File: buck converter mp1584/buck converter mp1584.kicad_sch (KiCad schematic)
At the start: 19 parts, among them J1 VIN, J2 GND, J3 VOUT, J4 GND

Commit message: First rough draft
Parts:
- added U1: ~, symbol buck converter module:mp1584
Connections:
- net FB: now also U1.4 (FB)
- net at C1.2, C11.2, C2.2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: now also U1.5 (GND)
- net at C1.1, C11.1, J1.1 (Pin_1)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: now also U1.7 (VIN)
- net BST: no longer names the net of C4.2
- net BST: now also U1.8 (BST)
- net COMP: no longer names the net of C3.1
- net COMP: now also U1.3 (COMP)
- net ENABLE: no longer names the net of R5.2, R6.1
- net ENABLE: now also U1.2 (EN)
- net FREQ: no longer names the net of R4.1
- net FREQ: now also U1.6 (FREQ)
- net SW: no longer names the net of C4.1, D1.1 (K), L1.1
- net SW: now also U1.1 (SW)
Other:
- moved on the sheet: R4, R5
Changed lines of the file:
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@@
   (junction (at 222.25 154.94) (diameter 0) (color 0 0 0 0)
   )
-  (junction (at 92.71 154.94) (diameter 0) (color 0 0 0 0)
+  (junction (at 78.74 154.94) (diameter 0) (color 0 0 0 0)
   )
   (junction (at 198.12 59.69) (diameter 0) (color 0 0 0 0)
@@
   (junction (at 49.53 154.94) (diameter 0) (color 0 0 0 0)
   )
-  (junction (at 63.5 105.41) (diameter 0) (color 0 0 0 0)
+  (junction (at 63.5 59.69) (diameter 0) (color 0 0 0 0)
   )
   (junction (at 198.12 154.94) (diameter 0) (color 0 0 0 0)
@@
   (junction (at 161.29 154.94) (diameter 0) (color 0 0 0 0)
   )
+  (junction (at 100.33 154.94) (diameter 0) (color 0 0 0 0)
+  )
   (junction (at 63.5 154.94) (diameter 0) (color 0 0 0 0)
   )
+  (junction (at 63.5 86.36) (diameter 0) (color 0 0 0 0)
+  )
   (no_connect (at 186.69 96.52))
-  (wire (pts (xy 92.71 115.57) (xy 92.71 124.46))
-    (stroke (width 0) (type default))
-  )
-  (wire (pts (xy 63.5 105.41) (xy 71.12 105.41))
+  (wire (pts (xy 78.74 99.06) (xy 78.74 124.46))
     (stroke (width 0) (type default))
   )
@@
     (stroke (width 0) (type default))
   )
-  (wire (pts (xy 144.78 82.55) (xy 133.35 82.55))
-    (stroke (width 0) (type default))
-  )
   (wire (pts (xy 186.69 59.69) (xy 198.12 59.69))
     (stroke (width 0) (type default))
@@
     (stroke (width 0) (type default))
   )
-  (wire (pts (xy 138.43 111.76) (xy 137.16 111.76))
+  (wire (pts (xy 144.78 92.71) (xy 113.03 92.71))
     (stroke (width 0) (type default))
   )
@@
     (stroke (width 0) (type default))
   )
-  (wire (pts (xy 63.5 85.09) (xy 63.5 105.41))
-    (stroke (width 0) (type default))
-  )
-  (wire (pts (xy 92.71 132.08) (xy 92.71 154.94))
+  (wire (pts (xy 100.33 154.94) (xy 138.43 154.94))
+    (stroke (width 0) (type default))
+  )
+  (wire (pts (xy 78.74 132.08) (xy 78.74 154.94))
+    (stroke (width 0) (type default))
+  )
+  (wire (pts (xy 63.5 59.69) (xy 100.33 59.69))
+    (stroke (width 0) (type default))
+  )
+  (wire (pts (xy 63.5 86.36) (xy 87.63 86.36))
     (stroke (width 0) (type default))
   )
@@
     (stroke (width 0) (type default))
   )
-  (wire (pts (xy 138.43 120.65) (xy 138.43 111.76))
+  (wire (pts (xy 138.43 99.06) (xy 138.43 120.65))
     (stroke (width 0) (type default))
   )
@@
     (stroke (width 0) (type default))
   )
-  (wire (pts (xy 63.5 59.69) (xy 63.5 77.47))
+  (wire (pts (xy 63.5 59.69) (xy 63.5 68.58))
     (stroke (width 0) (type default))
   )
@@
     (stroke (width 0) (type default))
   )
-  (wire (pts (xy 63.5 154.94) (xy 92.71 154.94))
+  (wire (pts (xy 63.5 154.94) (xy 78.74 154.94))
     (stroke (width 0) (type default))
   )
@@
     (stroke (width 0) (type default))
   )
+  (wire (pts (xy 113.03 99.06) (xy 138.43 99.06))
+    (stroke (width 0) (type default))
+  )
   (wire (pts (xy 36.83 154.94) (xy 49.53 154.94))
     (stroke (width 0) (type default))
@@
     (stroke (width 0) (type default))
   )
+  (wire (pts (xy 63.5 86.36) (xy 63.5 123.19))
+    (stroke (width 0) (type default))
+  )
+  (wire (pts (xy 100.33 59.69) (xy 100.33 77.47))
+    (stroke (width 0) (type default))
+  )
   (wire (pts (xy 27.94 59.69) (xy 36.83 59.69))
     (stroke (width 0) (type default))
@@
     (stroke (width 0) (type default))
   )
-  (wire (pts (xy 92.71 154.94) (xy 138.43 154.94))
+  (wire (pts (xy 133.35 86.36) (xy 113.03 86.36))
+    (stroke (width 0) (type default))
+  )
+  (wire (pts (xy 100.33 107.95) (xy 100.33 154.94))
+    (stroke (width 0) (type default))
+  )
+  (wire (pts (xy 78.74 154.94) (xy 100.33 154.94))
     (stroke (width 0) (type default))
   )
@@
     (stroke (width 0) (type default))
   )
-  (wire (pts (xy 144.78 74.93) (xy 144.78 82.55))
+  (wire (pts (xy 81.28 92.71) (xy 87.63 92.71))
+    (stroke (width 0) (type default))
+  )
+  (wire (pts (xy 133.35 59.69) (xy 133.35 86.36))
+    (stroke (width 0) (type default))
+  )
+  (wire (pts (xy 144.78 74.93) (xy 144.78 92.71))
     (stroke (width 0) (type default))
   )
@@
     (stroke (width 0) (type default))
   )
-  (wire (pts (xy 63.5 105.41) (xy 63.5 123.19))
+  (wire (pts (xy 78.74 99.06) (xy 87.63 99.06))
+    (stroke (width 0) (type default))
+  )
+  (wire (pts (xy 63.5 76.2) (xy 63.5 86.36))
     (stroke (width 0) (type default))
   )
@@
     (stroke (width 0) (type default))
   )
-  (global_label "BST" (shape input) (at 133.35 82.55 180) (fields_autoplaced)
+  (global_label "FB" (shape input) (at 81.28 92.71 180) (fields_autoplaced)
     (effects (font (size 1.27 1.27)) (justify right))
-    (property "Intersheetrefs" "${INTERSHEET_REFS}" (at 126.9177 82.55 0)
+    (property "Intersheetrefs" "${INTERSHEET_REFS}" (at 75.9362 92.71 0)
       (effects (font (size 1.27 1.27)) (justify right) hide)
     )
@@
     )
   )
-  (global_label "ENABLE" (shape input) (at 71.12 105.41 0) (fields_autoplaced)
-    (effects (font (size 1.27 1.27)) (justify left))
-    (property "Intersheetrefs" "${INTERSHEET_REFS}" (at 81.1204 105.41 0)
-      (effects (font (size 1.27 1.27)) (justify left) hide)
-    )
-  )
-  (global_label "FREQ" (shape input) (at 92.71 115.57 0) (fields_autoplaced)
-    (effects (font (size 1.27 1.27)) (justify left))
-    (property "Intersheetrefs" "${INTERSHEET_REFS}" (at 100.5333 115.57 0)
-      (effects (font (size 1.27 1.27)) (justify left) hide)
-    )
-  )
-  (global_label "COMP" (shape input) (at 137.16 111.76 180) (fields_autoplaced)
-    (effects (font (size 1.27 1.27)) (justify right))
-    (property "Intersheetrefs" "${INTERSHEET_REFS}" (at 128.8529 111.76 0)
-      (effects (font (size 1.27 1.27)) (justify right) hide)
-    )
-  )
-  (global_label "SW" (shape input) (at 133.35 59.69 180) (fields_autoplaced)
-    (effects (font (size 1.27 1.27)) (justify right))
-    (property "Intersheetrefs" "${INTERSHEET_REFS}" (at 127.7039 59.69 0)
-      (effects (font (size 1.27 1.27)) (justify right) hide)
-    )
-  )
   (symbol (lib_id "Device:R_Potentiometer") (at 186.69 92.71 0) (unit 1)
     (in_bom yes) (on_board yes) (dnp no) (fields_autoplaced)
@@
     )
   )
+  (symbol (lib_id "buck converter module:mp1584") (at 100.33 92.71 0) (unit 1)
+    (in_bom yes) (on_board yes) (dnp no) (fields_autoplaced)
+    (property "Reference" "U1" (at 102.5241 77.47 0)
+      (effects (font (size 1.27 1.27)) (justify left))
+    )
+    (property "Value" "~" (at 90.17 77.47 0)
+      (effects (font (size 1.27 1.27)))
+    )
+    (property "Footprint" "" (at 90.17 77.47 0)
+      (effects (font (size 1.27 1.27)) hide)
+    )
+    (property "Datasheet" "" (at 90.17 77.47 0)
+      (effects (font (size 1.27 1.27)) hide)
+    )
+    (pin "1")
+    (pin "2")
+    (pin "3")
+    (pin "4")
+    (pin "5")
+    (pin "6")
+    (pin "7")
+    (pin "8")
+    (instances
+      (project "buck converter mp1584"
+        (path "/961da25c-d60c-449f-8d16-769ca9c63dc4"
+          (reference "U1") (unit 1)
+        )
+      )
+    )
+  )
   (symbol (lib_id "Device:D") (at 161.29 71.12 270) (unit 1)
     (in_bom yes) (on_board yes) (dnp no) (fields_autoplaced)
@@
     )
   )
-  (symbol (lib_id "Device:R_US") (at 92.71 128.27 0) (unit 1)
-    (in_bom yes) (on_board yes) (dnp no)
-    (property "Reference" "R4" (at 95.25 128.27 90)
-      (effects (font (size 1.27 1.27)))
-    )
-    (property "Value" "R_US" (at 90.17 128.27 90)
-      (effects (font (size 1.27 1.27)))
-    )
-    (property "Footprint" "" (at 93.726 128.524 90)
-      (effects (font (size 1.27 1.27)) hide)
-    )
-    (property "Datasheet" "~" (at 92.71 128.27 0)
+  (symbol (lib_id "Device:R_US") (at 78.74 128.27 0) (unit 1)
+    (in_bom yes) (on_board yes) (dnp no)
+    (property "Reference" "R4" (at 81.28 128.27 90)
+      (effects (font (size 1.27 1.27)))
+    )
+    (property "Value" "R_US" (at 76.2 128.27 90)
+      (effects (font (size 1.27 1.27)))
+    )
+    (property "Footprint" "" (at 79.756 128.524 90)
+      (effects (font (size 1.27 1.27)) hide)
+    )
+    (property "Datasheet" "~" (at 78.74 128.27 0)
       (effects (font (size 1.27 1.27)) hide)
     )
@@
     )
   )
-  (symbol (lib_id "Device:R_US") (at 63.5 81.28 0) (unit 1)
-    (in_bom yes) (on_board yes) (dnp no)
-    (property "Reference" "R5" (at 66.04 81.28 90)
-      (effects (font (size 1.27 1.27)))
-    )
-    (property "Value" "R_US" (at 60.96 81.28 90)
-      (effects (font (size 1.27 1.27)))
-    )
-    (property "Footprint" "" (at 64.516 81.534 90)
-      (effects (font (size 1.27 1.27)) hide)
-    )
-    (property "Datasheet" "~" (at 63.5 81.28 0)
-      (effects (font (size 1.27 1.27)) hide)
-    )
+  (symbol (lib_id "Device:R_US") (at 63.5 72.39 0) (unit 1)
+    (in_bom yes) (on_board yes) (dnp no)
+    (property "Reference" "R5" (at 66.04 72.39 90)
+      (effects (font (size 1.27 1.27)))
+    )
+    (property "Value" "R_US" (at 60.96 72.39 90)
+      (effects (font (size 1.27 1.27)))
+    )
+    (property "Footprint" "" (at 64.516 72.644 90)
+      (effects (font (size 1.27 1.27)) hide)
+    )
+    (property "Datasheet" "~" (at 63.5 72.39 0)
+      (effects (font (size 1.27 1.27)) hide)
+    )

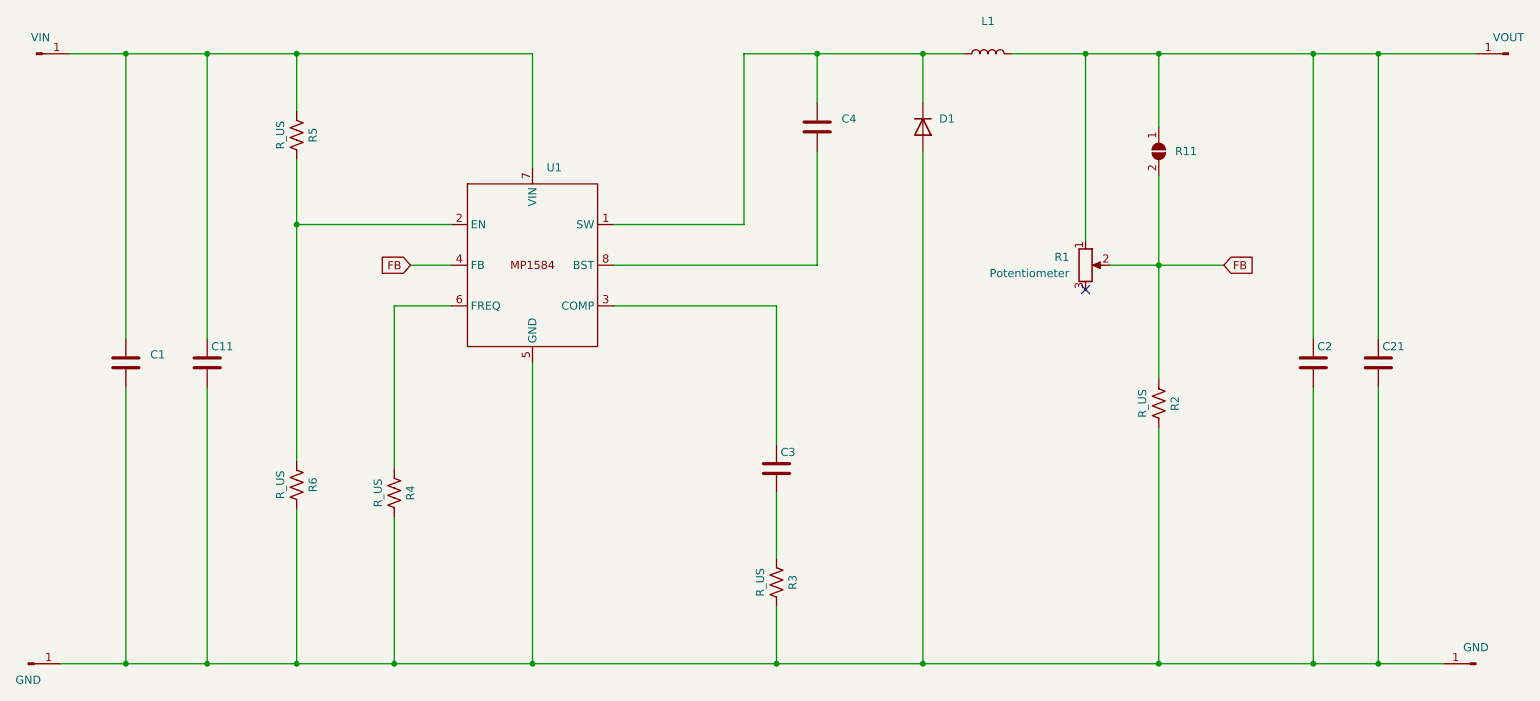
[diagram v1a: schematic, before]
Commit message: Tighten up layout
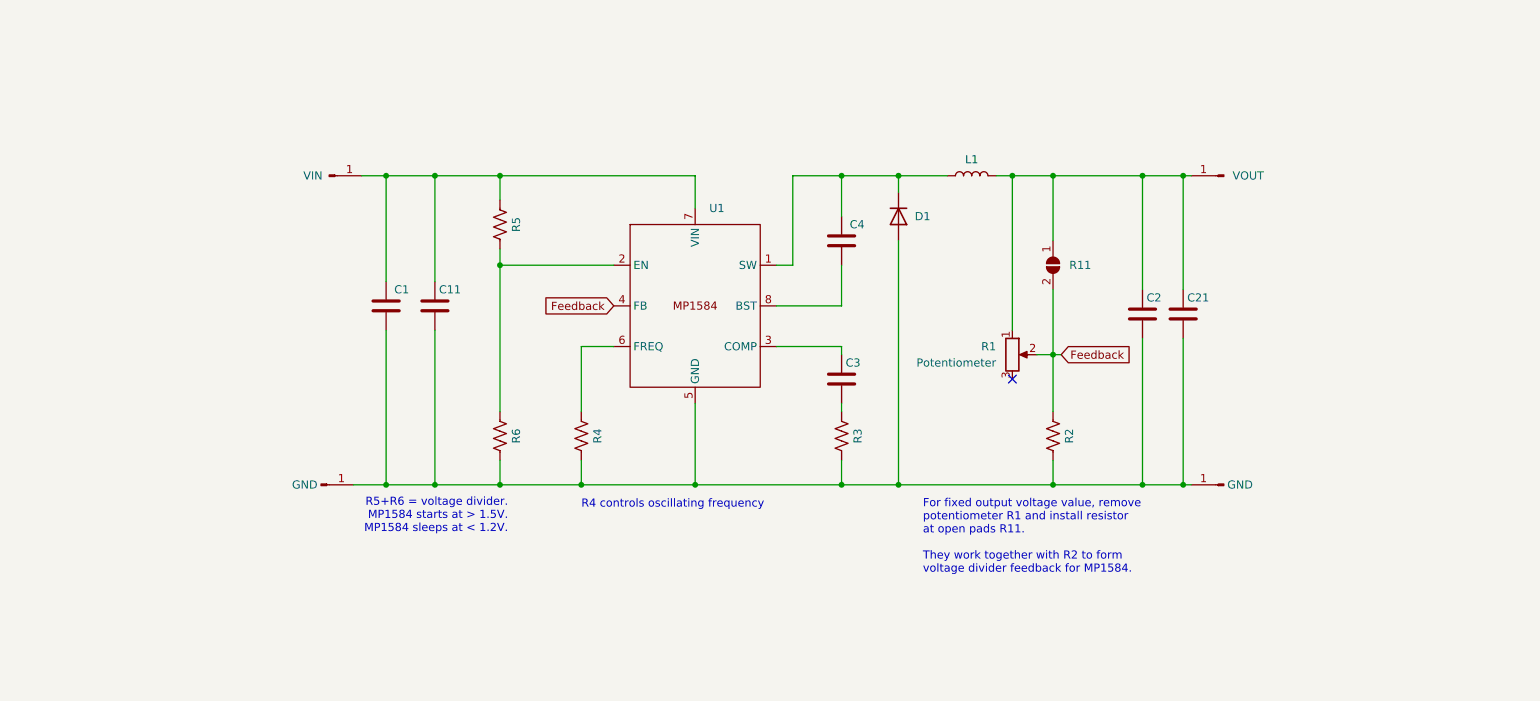
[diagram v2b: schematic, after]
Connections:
- net FB renamed Feedback
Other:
- note added: "For fixed output voltage value, remove potentiometer R1 and install resistor at open pads R11. They work together with R2 to form voltage divider feedback for MP1584."
- note added: "R4 controls oscillating frequency"
- note added: "R5+R6 = voltage divider. MP1584 starts at > 1.5V. MP1584 sleeps at < 1.2V."
- moved on the sheet: C1, C11, C2, C21, C3, C4, D1, L1, R1, R11, R2, R3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
